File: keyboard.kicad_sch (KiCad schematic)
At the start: 104 parts

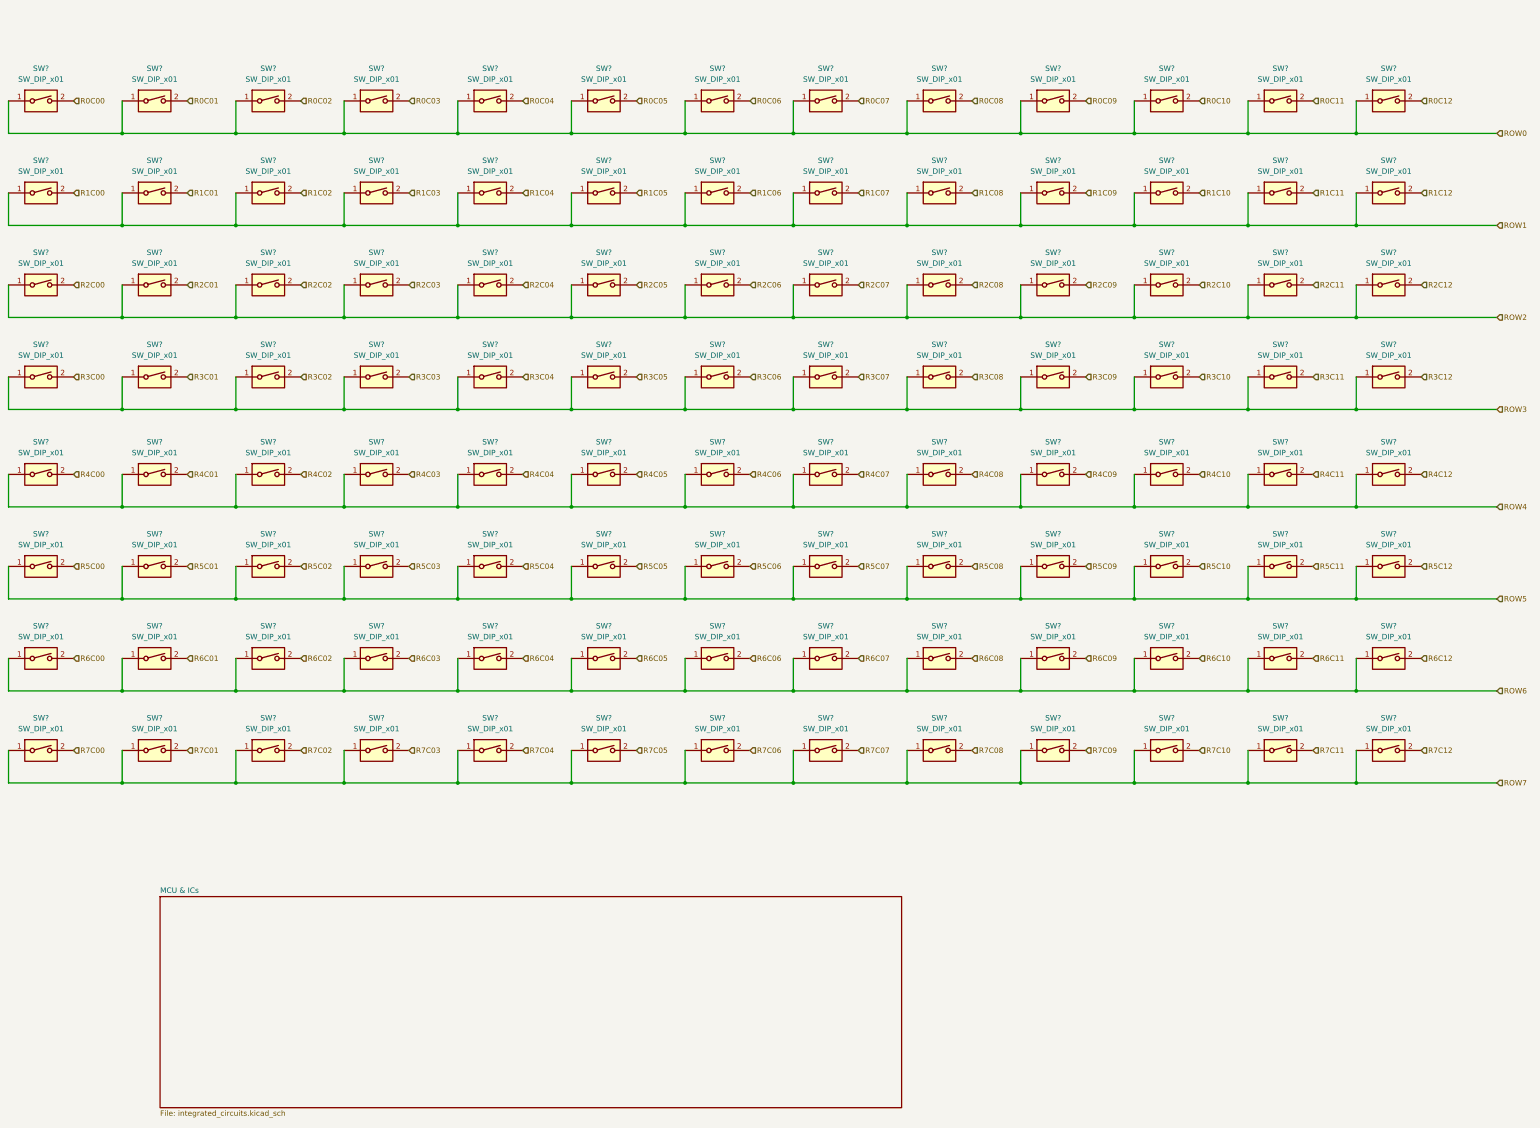
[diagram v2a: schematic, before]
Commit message: Add datasheet for ATSAM4S4BA-AUR MCU
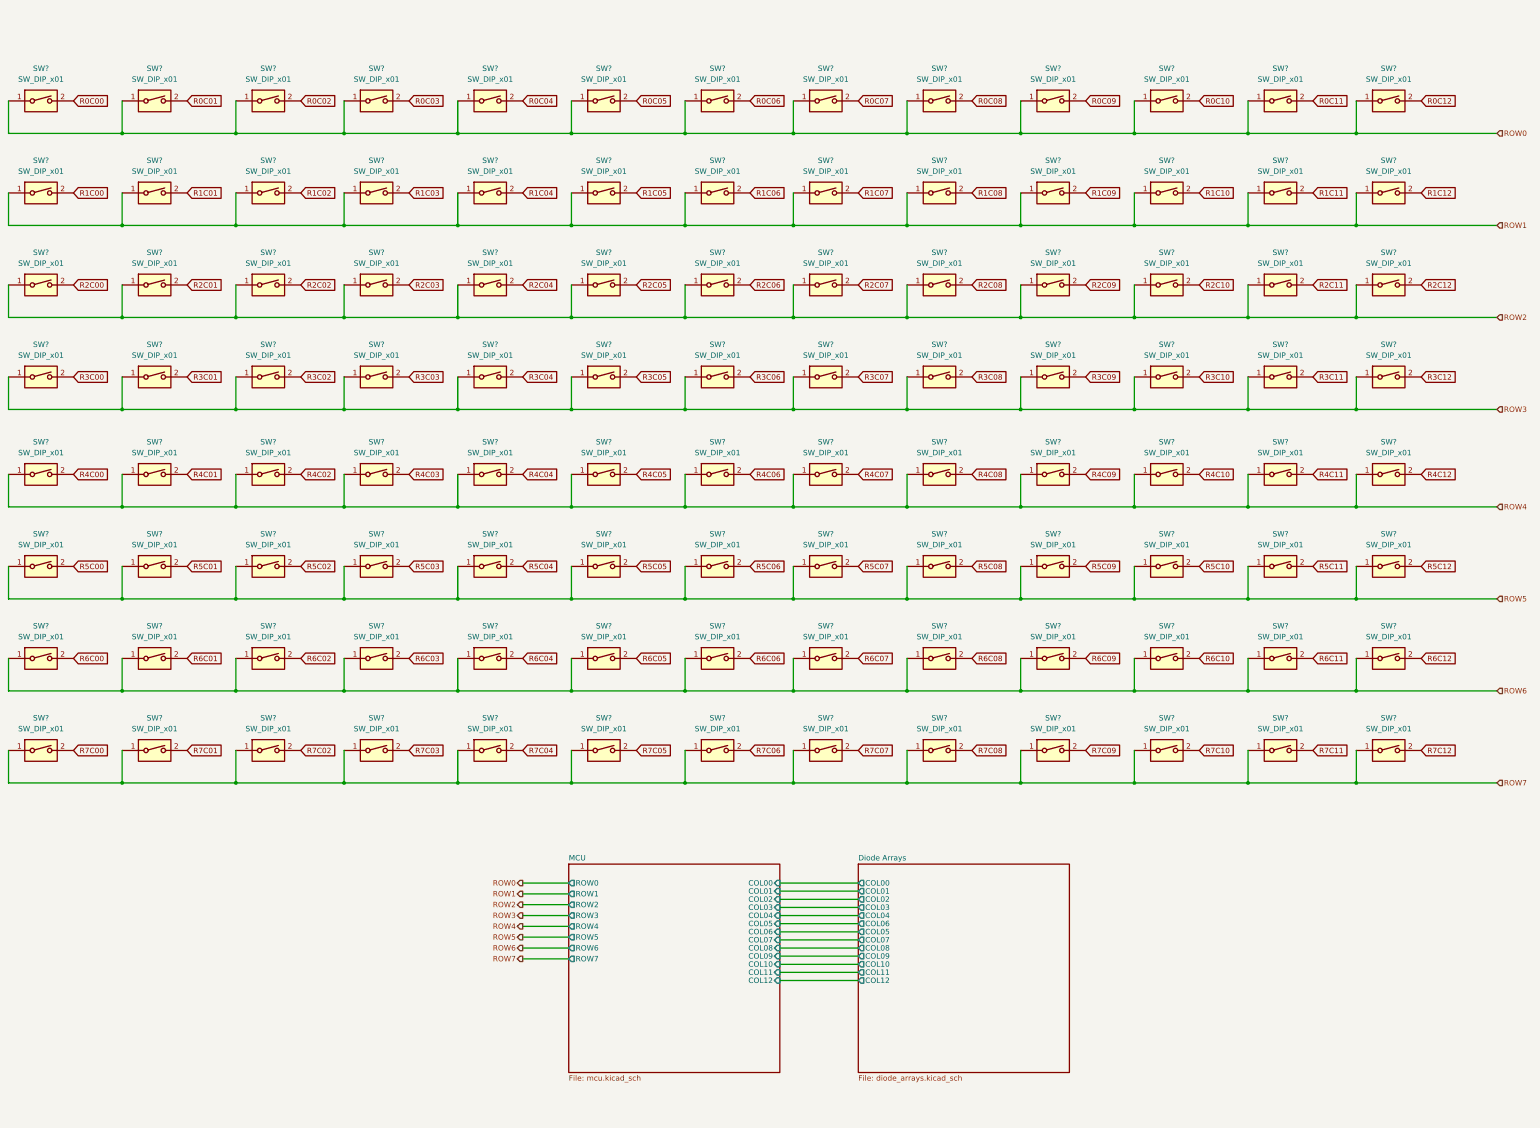
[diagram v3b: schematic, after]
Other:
- sheet MCU & ICs renamed Diode Arrays
- added sheet MCU (mcu.kicad_sch)
- sheet Diode Arrays: file integrated_circuits.kicad_sch -> diode_arrays.kicad_sch
- sheet Diode Arrays ports: added COL00, COL01, COL02, COL03, COL04, COL05, COL06, COL07, COL08, COL09, COL10, COL11, COL12; removed none

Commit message: Add vol switches
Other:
- note added: "Switch matrix"
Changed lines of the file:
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@@
     (stroke (width 0) (type default) (color 0 0 0 0))
+  )
+  (text "Switch matrix" (at 198.12 29.845 0)
+    (effects (font (size 5 5)) (justify left bottom))
   )
   (global_label "R2C08" (shape input) (at 270.51 86.36 0)
@@
   )
   (symbol_instances
-    (path "/9e0c78dd-5d55-4e6a-a58b-ab669270d485/3c272cb2-1c26-43ca-9023-35d88386f380"
+    (path "/9e0c78dd-5d55-4e6a-a58b-ab669270d485/1c96fb1a-816b-4937-b0f2-19c22d6d5200"
+      (reference "#PWR?") (unit 1) (value "VDD") (footprint "")
+    )
+    (path "/9e0c78dd-5d55-4e6a-a58b-ab669270d485/1db9a1da-ce57-4844-bdab-c12c3cad5196"
+      (reference "#PWR?") (unit 1) (value "VDD") (footprint "")
+    )
+    (path "/9e0c78dd-5d55-4e6a-a58b-ab669270d485/1f6144b1-4286-4293-b4d6-b174fee94260"
+      (reference "#PWR?") (unit 1) (value "VDD") (footprint "")
+    )
+    (path "/9e0c78dd-5d55-4e6a-a58b-ab669270d485/49c99316-771a-4d89-912a-7f1580eb8431"
       (reference "#PWR?") (unit 1) (value "VDD") (footprint "")
     )
@@
       (reference "#PWR?") (unit 1) (value "GND") (footprint "")
     )
-    (path "/9e0c78dd-5d55-4e6a-a58b-ab669270d485/6c679bb3-4cfb-4701-93f3-2ccdd14380ac"
+    (path "/9e0c78dd-5d55-4e6a-a58b-ab669270d485/55c61934-1dba-48ed-835b-12039ef9ba1a"
       (reference "#PWR?") (unit 1) (value "GND") (footprint "")
+    )
+    (path "/9e0c78dd-5d55-4e6a-a58b-ab669270d485/5e45d272-2275-4462-b25b-6fb6f9ce79ae"
+      (reference "#PWR?") (unit 1) (value "VDD") (footprint "")
+    )
+    (path "/9e0c78dd-5d55-4e6a-a58b-ab669270d485/7678549a-b100-43a1-a5ae-1e2ec9d2c7e3"
+      (reference "#PWR?") (unit 1) (value "GND") (footprint "")
+    )
+    (path "/9e0c78dd-5d55-4e6a-a58b-ab669270d485/8974272a-9a9a-41bf-b30d-43ca8ff0bf03"
+      (reference "#PWR?") (unit 1) (value "GND") (footprint "")
+    )
+    (path "/9e0c78dd-5d55-4e6a-a58b-ab669270d485/8ce8488f-b655-4f0d-bd28-47d11af3e2fb"
+      (reference "#PWR?") (unit 1) (value "GND") (footprint "")
+    )
+    (path "/9e0c78dd-5d55-4e6a-a58b-ab669270d485/a00050db-18c1-4736-a451-331c36c3a102"
+      (reference "#PWR?") (unit 1) (value "GND") (footprint "")
+    )
+    (path "/9e0c78dd-5d55-4e6a-a58b-ab669270d485/a23bb19e-cf7e-49dd-ba20-2b58c4a0cdaa"
+      (reference "#PWR?") (unit 1) (value "VDD") (footprint "")
+    )
+    (path "/9e0c78dd-5d55-4e6a-a58b-ab669270d485/a8aad9a4-b905-42ea-a506-c8f32ae3d6c8"
+      (reference "#PWR?") (unit 1) (value "VDD") (footprint "")
+    )
+    (path "/9e0c78dd-5d55-4e6a-a58b-ab669270d485/aee9babb-cd8b-4b48-ba9a-8f12a2c547f8"
+      (reference "#PWR?") (unit 1) (value "VBUS") (footprint "")
+    )
+    (path "/9e0c78dd-5d55-4e6a-a58b-ab669270d485/b1f2b439-5d5d-4c62-9102-b6f215989c8f"
+      (reference "#PWR?") (unit 1) (value "VDD") (footprint "")
     )
     (path "/9e0c78dd-5d55-4e6a-a58b-ab669270d485/b806580f-80a8-4636-b816-9de86dbbd3fc"
       (reference "#PWR?") (unit 1) (value "GND") (footprint "")
     )
-    (path "/9e0c78dd-5d55-4e6a-a58b-ab669270d485/e0c85bed-4ca1-4954-968e-e7da54799150"
-      (reference "#PWR?") (unit 1) (value "VDD") (footprint "")
+    (path "/9e0c78dd-5d55-4e6a-a58b-ab669270d485/ba99ab3b-ab04-42f1-bdeb-1249dc598c4c"
+      (reference "#PWR?") (unit 1) (value "GND") (footprint "")
+    )
+    (path "/9e0c78dd-5d55-4e6a-a58b-ab669270d485/c166788f-d628-41d0-8ddb-05505d3276f0"
+      (reference "#PWR?") (unit 1) (value "GND") (footprint "")
+    )
+    (path "/9e0c78dd-5d55-4e6a-a58b-ab669270d485/d690fb03-b0a4-485f-afe2-aeda27547596"
+      (reference "#PWR?") (unit 1) (value "GND") (footprint "")
+    )
+    (path "/9e0c78dd-5d55-4e6a-a58b-ab669270d485/ebf6df76-7541-4cfb-ba2d-1012d19dd58c"
+      (reference "#PWR?") (unit 1) (value "GND") (footprint "")
+    )
+    (path "/9e0c78dd-5d55-4e6a-a58b-ab669270d485/f3c7c4a5-d619-4ef9-b799-06ce472b2e74"
+      (reference "#PWR?") (unit 1) (value "GND") (footprint "")
+    )
+    (path "/9e0c78dd-5d55-4e6a-a58b-ab669270d485/fb1906e6-cc55-4cba-a220-83d48f6bf68b"
+      (reference "#PWR?") (unit 1) (value "VBUS") (footprint "")
+    )
+    (path "/9e0c78dd-5d55-4e6a-a58b-ab669270d485/fecc99a2-b45c-457d-869c-fa72ee3c6f2d"
+      (reference "#PWR?") (unit 1) (value "GND") (footprint "")
+    )
+    (path "/9e0c78dd-5d55-4e6a-a58b-ab669270d485/11fed8e5-5fb0-4411-826e-77406c80e7bd"
+      (reference "C?") (unit 1) (value "2.2u") (footprint "")
+    )
+    (path "/9e0c78dd-5d55-4e6a-a58b-ab669270d485/3ba861e6-2da8-4563-bab5-fe00ad08ce06"
+      (reference "C?") (unit 1) (value "1u") (footprint "")
+    )
+    (path "/9e0c78dd-5d55-4e6a-a58b-ab669270d485/48b360ce-0a8e-47e2-b7b3-ed76afa25553"
+      (reference "C?") (unit 1) (value "22p") (footprint "")
+    )
+    (path "/9e0c78dd-5d55-4e6a-a58b-ab669270d485/5a0414fb-7659-42d1-953b-9392dee32d2a"
+      (reference "C?") (unit 1) (value "100n") (footprint "")
+    )
+    (path "/9e0c78dd-5d55-4e6a-a58b-ab669270d485/626b75e9-3ee5-4480-ab77-93f67205bdc0"
+      (reference "C?") (unit 1) (value "4.7u") (footprint "")
+    )
+    (path "/9e0c78dd-5d55-4e6a-a58b-ab669270d485/917033a0-4769-4bae-8967-5b2bebee1e29"
+      (reference "C?") (unit 1) (value "1u") (footprint "")
+    )
+    (path "/9e0c78dd-5d55-4e6a-a58b-ab669270d485/fa135c27-276c-42d8-a7d7-d2aa6c4e0f0c"
+      (reference "C?") (unit 1) (value "22p") (footprint "")
     )
     (path "/9e0c78dd-5d55-4e6a-a58b-ab669270d485/84a09a01-2ef6-49bb-be4c-94b276821b3b"
@@
       (reference "D?") (unit 1) (value "LED") (footprint "")
     )
-    (path "/9e0c78dd-5d55-4e6a-a58b-ab669270d485/e5aa98ce-6ab0-49f4-93ab-735d8eb24e17"
+    (path "/9e0c78dd-5d55-4e6a-a58b-ab669270d485/79bf98bd-c0fc-450d-a86a-b29531f20dc5"
       (reference "J?") (unit 1) (value "USB_C_Receptacle_USB2.0") (footprint "")
+    )
+    (path "/9e0c78dd-5d55-4e6a-a58b-ab669270d485/01b79ee4-9737-4721-be1a-42bae027db1a"
+      (reference "R?") (unit 1) (value "56K") (footprint "")
+    )
+    (path "/9e0c78dd-5d55-4e6a-a58b-ab669270d485/15419263-ae95-4408-bb7a-26842f0d6d79"
+      (reference "R?") (unit 1) (value "10K") (footprint "")
+    )
+    (path "/9e0c78dd-5d55-4e6a-a58b-ab669270d485/54060d77-4c31-4584-845f-eab70f04b82b"
+      (reference "R?") (unit 1) (value "10K") (footprint "")
+    )
+    (path "/9e0c78dd-5d55-4e6a-a58b-ab669270d485/5c8ca59e-5148-4b7c-877b-a44c270148f5"
+      (reference "R?") (unit 1) (value "56K") (footprint "")
     )
     (path "/9e0c78dd-5d55-4e6a-a58b-ab669270d485/9c406405-a624-4002-a0b7-d220d69a76d9"
       (reference "R?") (unit 1) (value "220") (footprint "")
     )
+    (path "/9e0c78dd-5d55-4e6a-a58b-ab669270d485/9edc7ee4-b20c-4420-9a61-fca0ad277a7a"
+      (reference "R?") (unit 1) (value "27") (footprint "")
+    )
     (path "/9e0c78dd-5d55-4e6a-a58b-ab669270d485/a19e659d-abc3-46cf-8f19-53ac2cd752de"
       (reference "R?") (unit 1) (value "220") (footprint "")
     )
+    (path "/9e0c78dd-5d55-4e6a-a58b-ab669270d485/b1ffbb1c-f03f-4f70-ad24-e558328ddfe9"
+      (reference "R?") (unit 1) (value "27") (footprint "")
+    )
+    (path "/9e0c78dd-5d55-4e6a-a58b-ab669270d485/f68e7ff3-5913-4e3d-9b66-11059bc8e6f7"
+      (reference "R?") (unit 1) (value "10K") (footprint "")
+    )
     (path "/9e0c78dd-5d55-4e6a-a58b-ab669270d485/fa90c4da-5c50-44e2-8823-0fcc7f8703e5"
       (reference "R?") (unit 1) (value "220") (footprint "")
@@
       (reference "SW?") (unit 1) (value "SW_DIP_x01") (footprint "")
     )
+    (path "/9e0c78dd-5d55-4e6a-a58b-ab669270d485/49c7d7b1-6bc7-4b54-9dc6-bfa2f72977f6"
+      (reference "SW?") (unit 1) (value "SW_DIP_x01") (footprint "")
+    )
     (path "/49fcf459-4cc7-46b9-8168-57ad9a57cc25"
       (reference "SW?") (unit 1) (value "SW_DIP_x01") (footprint "")
@@
       (reference "SW?") (unit 1) (value "SW_DIP_x01") (footprint "")
     )
-    (path "/9e0c78dd-5d55-4e6a-a58b-ab669270d485/5fe496f0-1da7-4790-91d7-fc4b4769f4db"
-      (reference "SW?") (unit 1) (value "RotaryEncoder_Switch") (footprint "")
+    (path "/9e0c78dd-5d55-4e6a-a58b-ab669270d485/5fe589ea-3cf1-46b3-8382-2e682b269f17"
+      (reference "SW?") (unit 1) (value "RotaryEncoder") (footprint "")
     )
     (path "/654304e0-1a14-4891-a9c9-2034740fa33c"
@@
       (reference "SW?") (unit 1) (value "SW_DIP_x01") (footprint "")
     )
+    (path "/9e0c78dd-5d55-4e6a-a58b-ab669270d485/aa8e004f-446c-42a6-86de-3c88f2ede2d1"
+      (reference "SW?") (unit 1) (value "SW_DIP_x01") (footprint "")
+    )
     (path "/ac648043-336b-4157-b719-8038f4f5615b"
       (reference "SW?") (unit 1) (value "SW_DIP_x01") (footprint "")
@@
       (reference "SW?") (unit 1) (value "SW_DIP_x01") (footprint "")
     )
+    (path "/9e0c78dd-5d55-4e6a-a58b-ab669270d485/b2301261-f732-4593-999e-2141e93dc747"
+      (reference "SW?") (unit 1) (value "SW_DIP_x01") (footprint "")
+    )
     (path "/b47b0e7e-ea09-493e-993d-213a09418ca3"
       (reference "SW?") (unit 1) (value "SW_DIP_x01") (footprint "")
@@
     (path "/fe1b3bb1-e9c2-4d5c-99bc-3f611fd6af4d"
       (reference "SW?") (unit 1) (value "SW_DIP_x01") (footprint "")
+    )
+    (path "/9e0c78dd-5d55-4e6a-a58b-ab669270d485/1c983152-5f3b-4bd8-9687-4444748d89c1"
+      (reference "U?") (unit 1) (value "TLV1117LV") (footprint "")
     )
     (path "/7dc9c916-febc-4440-93a8-d6dc06c2aff1/20b6e50f-13e1-44f6-ad04-b0a948f35b30"
@@
       (reference "U?") (unit 1) (value "S16-4148") (footprint "")
     )
-  )
+    (path "/9e0c78dd-5d55-4e6a-a58b-ab669270d485/983d2e15-168f-42e2-a578-b185a713cff8"
+      (reference "Y?") (unit 1) (value "XTAL-12M") (footprint "")
+    )
+  )
